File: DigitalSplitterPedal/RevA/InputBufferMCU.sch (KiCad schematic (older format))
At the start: 4 parts, among them U7 MCP601-xOT

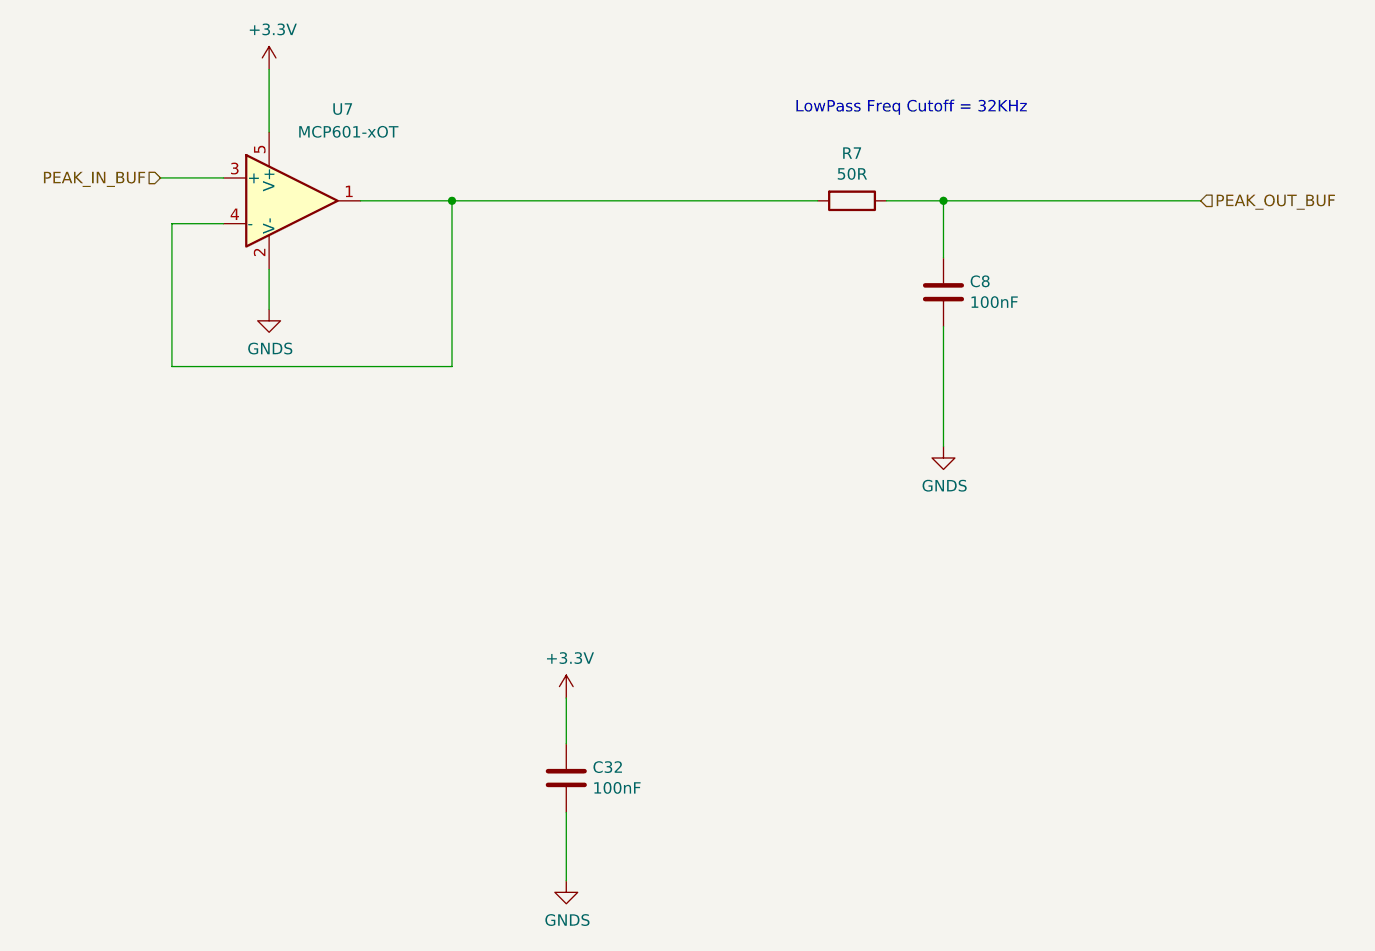
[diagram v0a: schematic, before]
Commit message: HW update
- Completed RevA layout (draft)
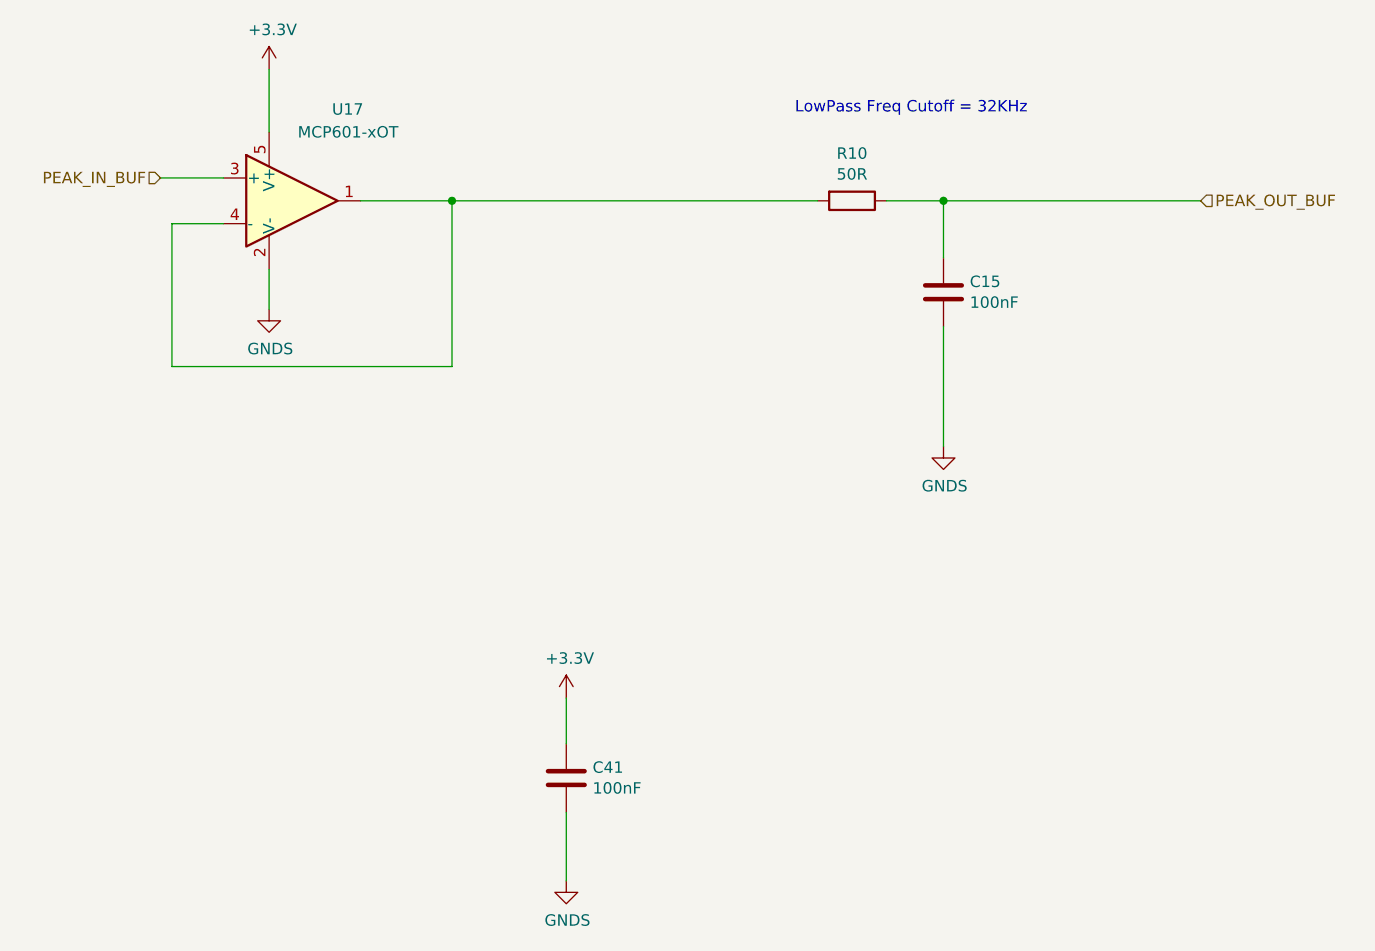
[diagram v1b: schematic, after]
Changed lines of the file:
@@
 AR Path="/5F6CB23D/5F7304B8/5F724E1F" Ref="U16"  Part="1"
 AR Path="/5F6CB23D/5F73168C/5F724E1F" Ref="U17"  Part="1"
-F 0 "U7" H 4425 3725 50  0000 L CNN
+F 0 "U17" H 4425 3725 50  0000 L CNN
 F 1 "MCP601-xOT" H 4275 3625 50  0000 L CNN
 F 2 "Package_TO_SOT_SMD:SOT-23-5" H 4150 3125 50  0001 L CNN
@@
 AR Path="/5F6CB23D/5F7304B8/5F724E26" Ref="#PWR016"  Part="1"
 AR Path="/5F6CB23D/5F73168C/5F724E26" Ref="#PWR020"  Part="1"
-F 0 "#PWR0125" H 4150 2600 50  0001 C CNN
+F 0 "#PWR020" H 4150 2600 50  0001 C CNN
 F 1 "+3.3V" H 4165 2923 50  0000 C CNN
 F 2 "" H 4150 2750 50  0001 C CNN
@@
 AR Path="/5F6CB23D/5F7304B8/5F724E33" Ref="#PWR017"  Part="1"
 AR Path="/5F6CB23D/5F73168C/5F724E33" Ref="#PWR021"  Part="1"
-F 0 "#PWR0126" H 4150 3550 50  0001 C CNN
+F 0 "#PWR021" H 4150 3550 50  0001 C CNN
 F 1 "GNDS" H 4155 3627 50  0000 C CNN
 F 2 "" H 4150 3800 50  0001 C CNN
@@
 AR Path="/5F6CB23D/5F7304B8/5F75A79C" Ref="C40"  Part="1"
 AR Path="/5F6CB23D/5F73168C/5F75A79C" Ref="C41"  Part="1"
-F 0 "C32" H 5565 5896 50  0000 L CNN
+F 0 "C41" H 5565 5896 50  0000 L CNN
 F 1 "100nF" H 5565 5805 50  0000 L CNN
 F 2 "Capacitor_SMD:C_0805_2012Metric_Pad1.15x1.40mm_HandSolder" H 5488 5700 50  0001 C CNN
@@
 AR Path="/5F6CB23D/5F7304B8/5F75A7C0" Ref="#PWR019"  Part="1"
 AR Path="/5F6CB23D/5F73168C/5F75A7C0" Ref="#PWR023"  Part="1"
-F 0 "#PWR013" H 5450 6050 50  0001 C CNN
+F 0 "#PWR023" H 5450 6050 50  0001 C CNN
 F 1 "GNDS" H 5455 6127 50  0000 C CNN
 F 2 "" H 5450 6300 50  0001 C CNN
@@
 AR Path="/5F6CB23D/5F7304B8/5F75A7C6" Ref="#PWR018"  Part="1"
 AR Path="/5F6CB23D/5F73168C/5F75A7C6" Ref="#PWR022"  Part="1"
-F 0 "#PWR012" H 5450 5350 50  0001 C CNN
+F 0 "#PWR022" H 5450 5350 50  0001 C CNN
 F 1 "+3.3V" H 5465 5673 50  0000 C CNN
 F 2 "" H 5450 5500 50  0001 C CNN
@@
 AR Path="/5F6CB23D/5F7304B8/5F86DDB1" Ref="R9"  Part="1"
 AR Path="/5F6CB23D/5F73168C/5F86DDB1" Ref="R10"  Part="1"
-F 0 "R7" V 6493 3325 50  0000 C CNN
+F 0 "R10" V 6493 3325 50  0000 C CNN
 F 1 "50R" V 6584 3325 50  0000 C CNN
 F 2 "Resistor_SMD:R_0805_2012Metric_Pad1.15x1.40mm_HandSolder" V 6630 3325 50  0001 C CNN
@@
 AR Path="/5F6CB23D/5F7304B8/5F86E25D" Ref="C10"  Part="1"
 AR Path="/5F6CB23D/5F73168C/5F86E25D" Ref="C15"  Part="1"
-F 0 "C8" H 7215 3771 50  0000 L CNN
+F 0 "C15" H 7215 3771 50  0000 L CNN
 F 1 "100nF" H 7215 3680 50  0000 L CNN
 F 2 "Capacitor_SMD:C_0805_2012Metric_Pad1.15x1.40mm_HandSolder" H 7138 3575 50  0001 C CNN
@@
 AR Path="/5F6CB23D/5F7304B8/5F86EBF7" Ref="#PWR05"  Part="1"
 AR Path="/5F6CB23D/5F73168C/5F86EBF7" Ref="#PWR025"  Part="1"
-F 0 "#PWR03" H 7100 4150 50  0001 C CNN
+F 0 "#PWR025" H 7100 4150 50  0001 C CNN
 F 1 "GNDS" H 7105 4227 50  0000 C CNN
 F 2 "" H 7100 4400 50  0001 C CNN

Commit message: updated hw
- add testpoints
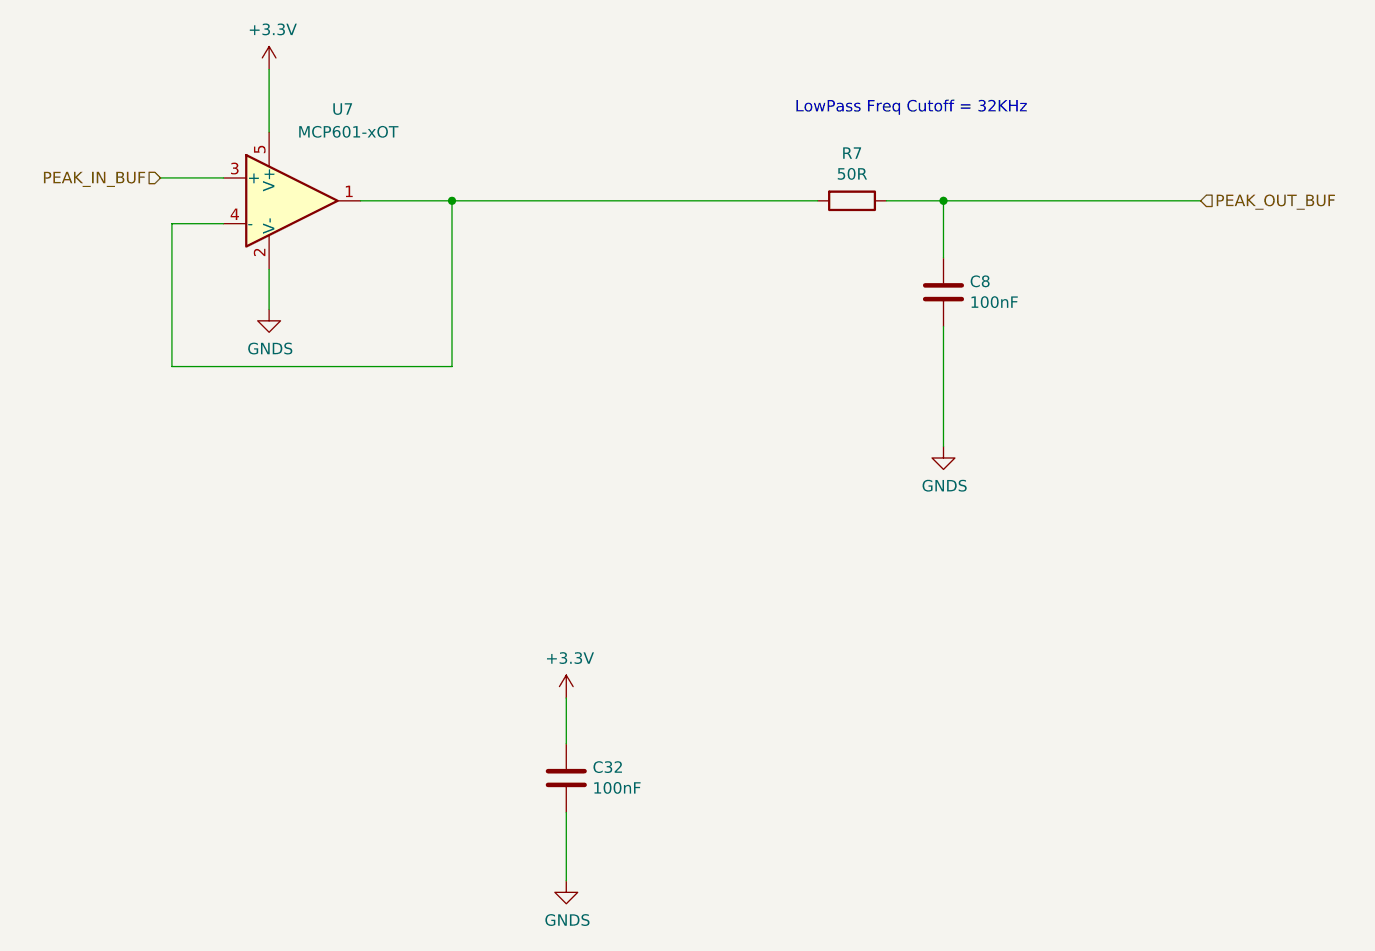
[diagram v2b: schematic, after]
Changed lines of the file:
@@
 $Descr A4 11693 8268
 encoding utf-8
-Sheet 10 15
+Sheet 8 15
 Title ""
 Date ""
@@
 AR Path="/5F6CB23D/5F7304B8/5F724E1F" Ref="U16"  Part="1"
 AR Path="/5F6CB23D/5F73168C/5F724E1F" Ref="U17"  Part="1"
-F 0 "U17" H 4425 3725 50  0000 L CNN
+F 0 "U7" H 4425 3725 50  0000 L CNN
 F 1 "MCP601-xOT" H 4275 3625 50  0000 L CNN
 F 2 "Package_TO_SOT_SMD:SOT-23-5" H 4150 3125 50  0001 L CNN
@@
 AR Path="/5F6CB23D/5F7304B8/5F724E26" Ref="#PWR016"  Part="1"
 AR Path="/5F6CB23D/5F73168C/5F724E26" Ref="#PWR020"  Part="1"
-F 0 "#PWR020" H 4150 2600 50  0001 C CNN
+F 0 "#PWR0125" H 4150 2600 50  0001 C CNN
 F 1 "+3.3V" H 4165 2923 50  0000 C CNN
 F 2 "" H 4150 2750 50  0001 C CNN
@@
 AR Path="/5F6CB23D/5F7304B8/5F724E33" Ref="#PWR017"  Part="1"
 AR Path="/5F6CB23D/5F73168C/5F724E33" Ref="#PWR021"  Part="1"
-F 0 "#PWR021" H 4150 3550 50  0001 C CNN
+F 0 "#PWR0126" H 4150 3550 50  0001 C CNN
 F 1 "GNDS" H 4155 3627 50  0000 C CNN
 F 2 "" H 4150 3800 50  0001 C CNN
@@
 AR Path="/5F6CB23D/5F7304B8/5F75A79C" Ref="C40"  Part="1"
 AR Path="/5F6CB23D/5F73168C/5F75A79C" Ref="C41"  Part="1"
-F 0 "C41" H 5565 5896 50  0000 L CNN
+F 0 "C32" H 5565 5896 50  0000 L CNN
 F 1 "100nF" H 5565 5805 50  0000 L CNN
 F 2 "Capacitor_SMD:C_0805_2012Metric_Pad1.15x1.40mm_HandSolder" H 5488 5700 50  0001 C CNN
@@
 AR Path="/5F6CB23D/5F7304B8/5F75A7C0" Ref="#PWR019"  Part="1"
 AR Path="/5F6CB23D/5F73168C/5F75A7C0" Ref="#PWR023"  Part="1"
-F 0 "#PWR023" H 5450 6050 50  0001 C CNN
+F 0 "#PWR013" H 5450 6050 50  0001 C CNN
 F 1 "GNDS" H 5455 6127 50  0000 C CNN
 F 2 "" H 5450 6300 50  0001 C CNN
@@
 AR Path="/5F6CB23D/5F7304B8/5F75A7C6" Ref="#PWR018"  Part="1"
 AR Path="/5F6CB23D/5F73168C/5F75A7C6" Ref="#PWR022"  Part="1"
-F 0 "#PWR022" H 5450 5350 50  0001 C CNN
+F 0 "#PWR012" H 5450 5350 50  0001 C CNN
 F 1 "+3.3V" H 5465 5673 50  0000 C CNN
 F 2 "" H 5450 5500 50  0001 C CNN
@@
 AR Path="/5F6CB23D/5F7304B8/5F86DDB1" Ref="R9"  Part="1"
 AR Path="/5F6CB23D/5F73168C/5F86DDB1" Ref="R10"  Part="1"
-F 0 "R10" V 6493 3325 50  0000 C CNN
+F 0 "R7" V 6493 3325 50  0000 C CNN
 F 1 "50R" V 6584 3325 50  0000 C CNN
 F 2 "Resistor_SMD:R_0805_2012Metric_Pad1.15x1.40mm_HandSolder" V 6630 3325 50  0001 C CNN
@@
 AR Path="/5F6CB23D/5F7304B8/5F86E25D" Ref="C10"  Part="1"
 AR Path="/5F6CB23D/5F73168C/5F86E25D" Ref="C15"  Part="1"
-F 0 "C15" H 7215 3771 50  0000 L CNN
+F 0 "C8" H 7215 3771 50  0000 L CNN
 F 1 "100nF" H 7215 3680 50  0000 L CNN
 F 2 "Capacitor_SMD:C_0805_2012Metric_Pad1.15x1.40mm_HandSolder" H 7138 3575 50  0001 C CNN
@@
 AR Path="/5F6CB23D/5F7304B8/5F86EBF7" Ref="#PWR05"  Part="1"
 AR Path="/5F6CB23D/5F73168C/5F86EBF7" Ref="#PWR025"  Part="1"
-F 0 "#PWR025" H 7100 4150 50  0001 C CNN
+F 0 "#PWR03" H 7100 4150 50  0001 C CNN
 F 1 "GNDS" H 7105 4227 50  0000 C CNN
 F 2 "" H 7100 4400 50  0001 C CNN
